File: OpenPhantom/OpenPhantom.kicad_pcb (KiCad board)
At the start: 2 copper layers, 175 x 175 mm, 108 parts, among them J1 Barrel_Jack, J2 Video, J3 Audio, Q1 BC548, Q2 BD136, Q3 BC557, Q4 BC548, SW1 POWER, SW2 RESET, U1 UM6116 VRAM, U10 74HC368, U11 74HC368, U2 UM6116 WRAM, U3 74HC04, U4 UA6547_CPU, U5 4013, U6 UA6548_PPU, U7 74HC139, U8 74LS373, U9 LM7805_TO220, Y1 21.453366 MHz

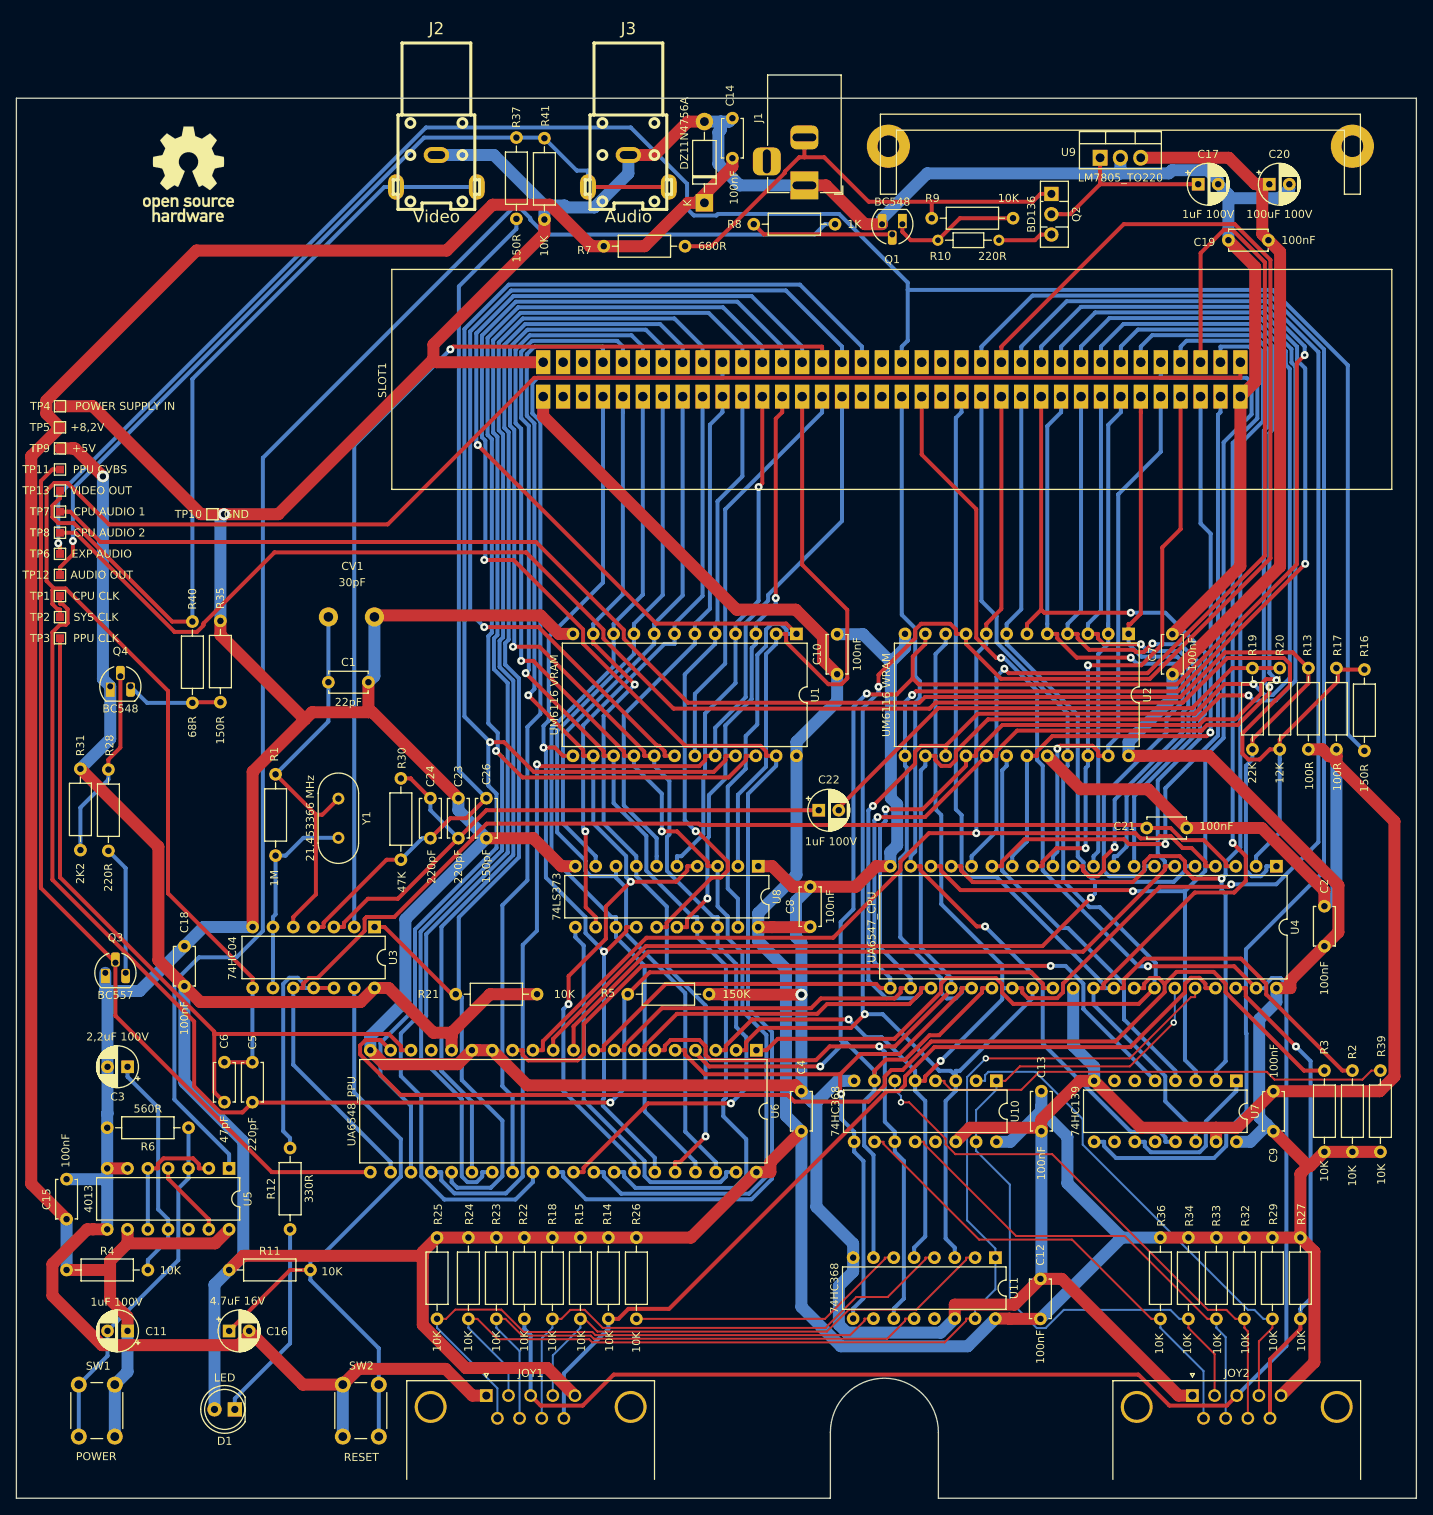
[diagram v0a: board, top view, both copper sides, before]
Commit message: Joy port fix.
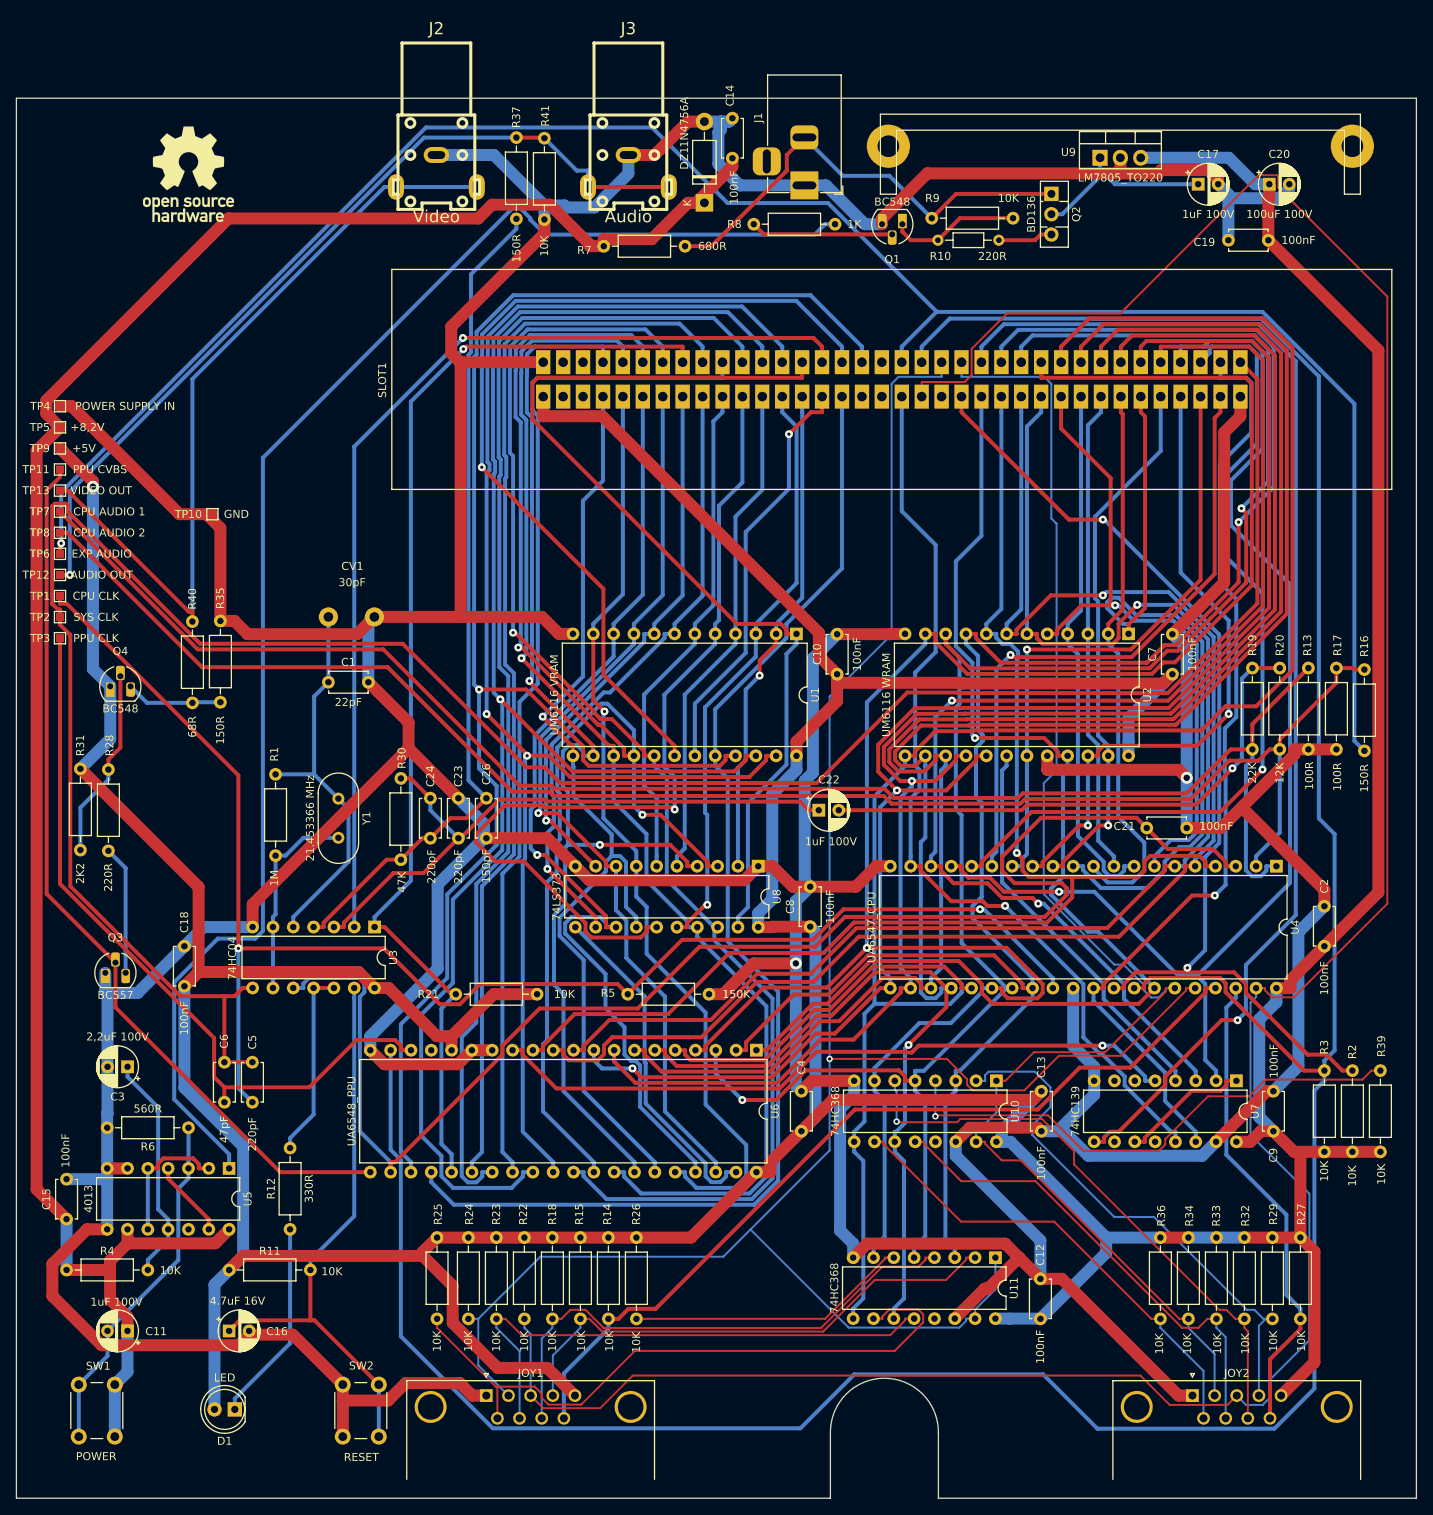
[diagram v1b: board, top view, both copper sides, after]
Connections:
- net /EXP-1 renamed /OUT-0
- SLOT1 pad 16: /EXP-0 -> unconnected-(SLOT1-Pad16)
- SLOT1 pad 19: /EXP-3 -> unconnected-(SLOT1-Pad19)
- SLOT1 pad 20: /EXP-4 -> unconnected-(SLOT1-Pad20)
- SLOT1 pad 51: /EXP-9 -> /~{INP1}
- SLOT1 pad 52: /EXP-8 -> /~{INP0}
- SLOT1 pad 53: /EXP-7 -> /~{NMI}
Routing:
- net /~{NMI}: track 147.4 -> 377.4 mm
- net /~{INP0}: track 144.1 -> 268.1 mm
- net /~{INP1}: track 96.0 -> 183.7 mm, vias 1 -> 0
- net /OUT-0: track 260.2 -> 341.7 mm, vias 2 -> 0
- net /GND: track 1063.4 -> 1007.8 mm
- net /CPU-D1: track 273.4 -> 229.7 mm, vias 3 -> 2
- net /SYSTEM-CLK: track 252.0 -> 295.3 mm
- net /PPU-A3: track 76.7 -> 112.7 mm
- net /PPU-A7: track 155.5 -> 124.6 mm, vias 1 -> 0
- net /CPU-A1: track 157.8 -> 182.8 mm
- net /AUDIO-2: track 226.4 -> 201.8 mm
- net /RST: track 158.2 -> 181.3 mm
- net /PPU-A8: track 205.6 -> 184.7 mm, vias 1 -> 2
- net /CPU-A12: track 126.5 -> 105.7 mm
- net /CPU-A7: track 75.0 -> 95.7 mm, vias 1 -> 0
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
